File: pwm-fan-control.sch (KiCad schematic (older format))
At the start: 26 parts, among them J1 Fan-out0, J2 PWM and power, J3 Fan-out1, Q1 Q_NMOS_GSD, Q2 Q_NMOS_GSD, Q3 MUN5211DW1, U1 LM358

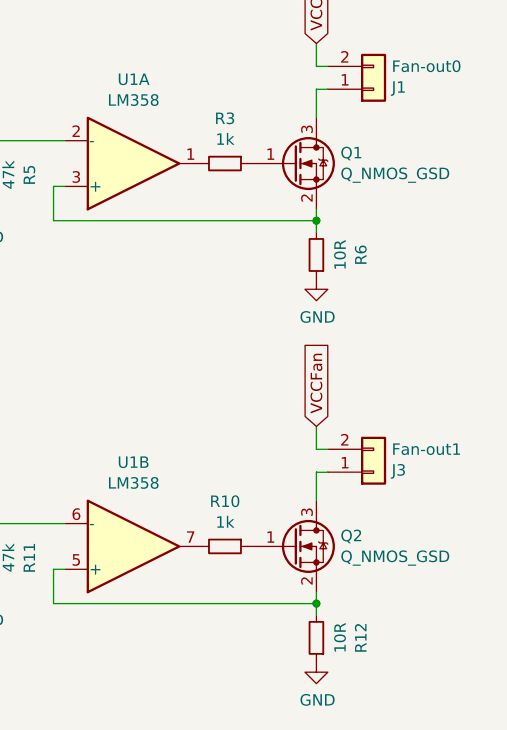
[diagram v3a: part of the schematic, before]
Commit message: Added model-numer to output transistors
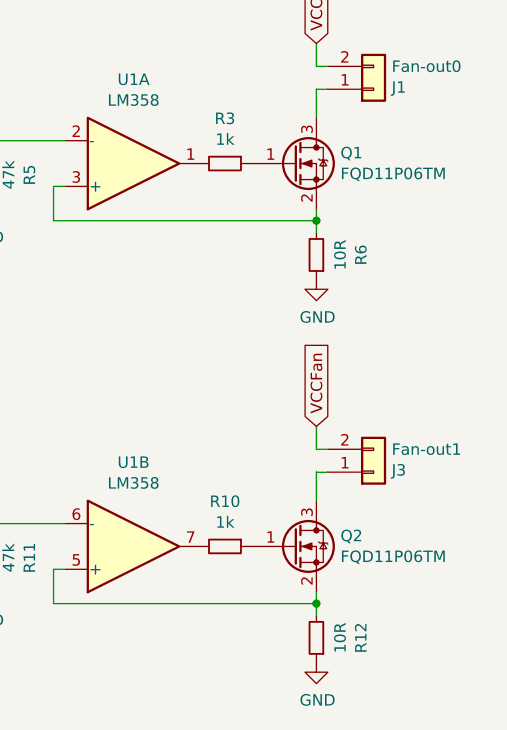
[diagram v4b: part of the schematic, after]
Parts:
- Q1, Q2: value Q_NMOS_GSD -> FQD11P06TM
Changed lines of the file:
@@
 P 6450 3450
 F 0 "Q1" H 6655 3496 50  0000 L CNN
-F 1 "Q_NMOS_GSD" H 6655 3405 50  0000 L CNN
+F 1 "FQD11P06TM" H 6655 3405 50  0000 L CNN
 F 2 "Package_TO_SOT_SMD:TO-252-2" H 6650 3550 50  0001 C CNN
 F 3 "~" H 6450 3450 50  0001 C CNN
@@
 P 6450 5125
 F 0 "Q2" H 6655 5171 50  0000 L CNN
-F 1 "Q_NMOS_GSD" H 6655 5080 50  0000 L CNN
+F 1 "FQD11P06TM" H 6655 5080 50  0000 L CNN
 F 2 "Package_TO_SOT_SMD:TO-252-2" H 6650 5225 50  0001 C CNN
 F 3 "~" H 6450 5125 50  0001 C CNN
